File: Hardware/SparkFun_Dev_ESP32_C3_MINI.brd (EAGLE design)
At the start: 21 x 36.1 mm, 88 parts, among them J1 USB Female Type C Connector, J5 Vertical Qwiic Connector, U1 ESP32-C3_MINI-1, U2 RT9080-33GJ5

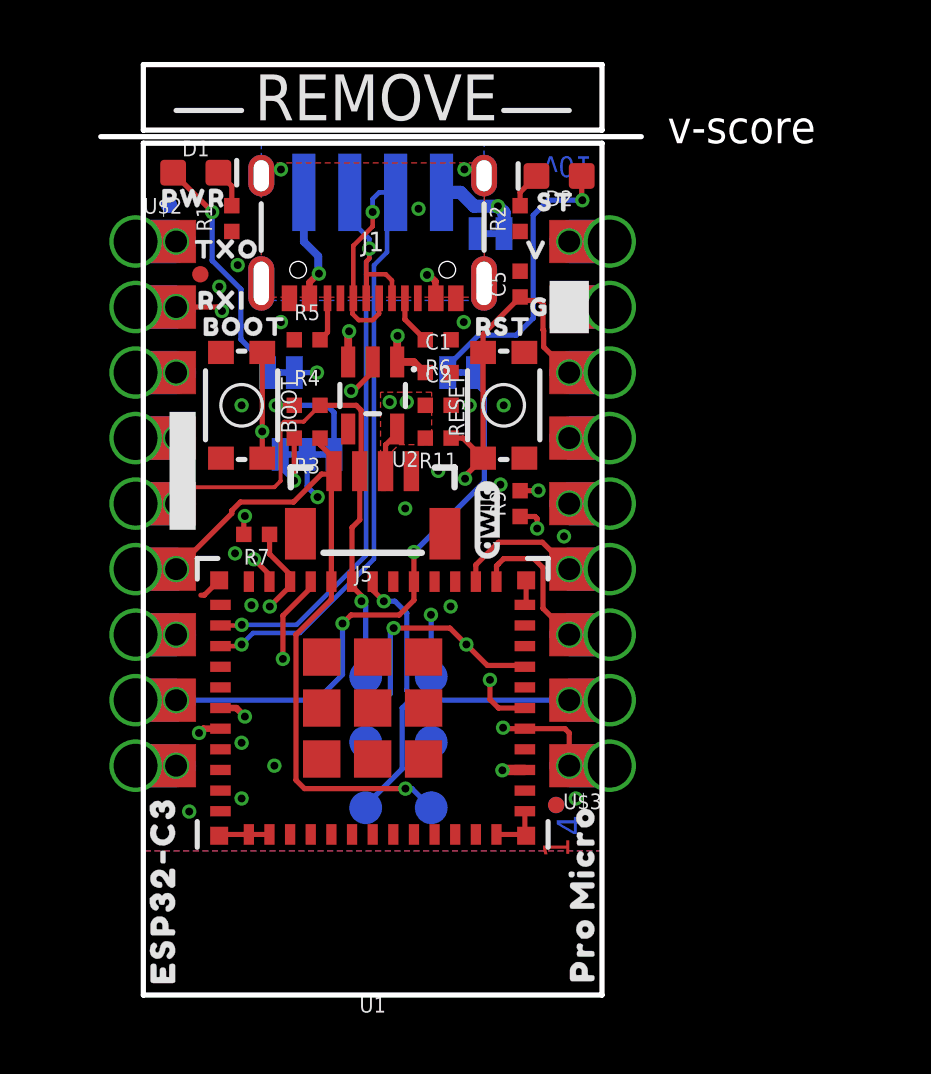
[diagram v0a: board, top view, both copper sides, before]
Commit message: Adds a few vias, cams prototypes
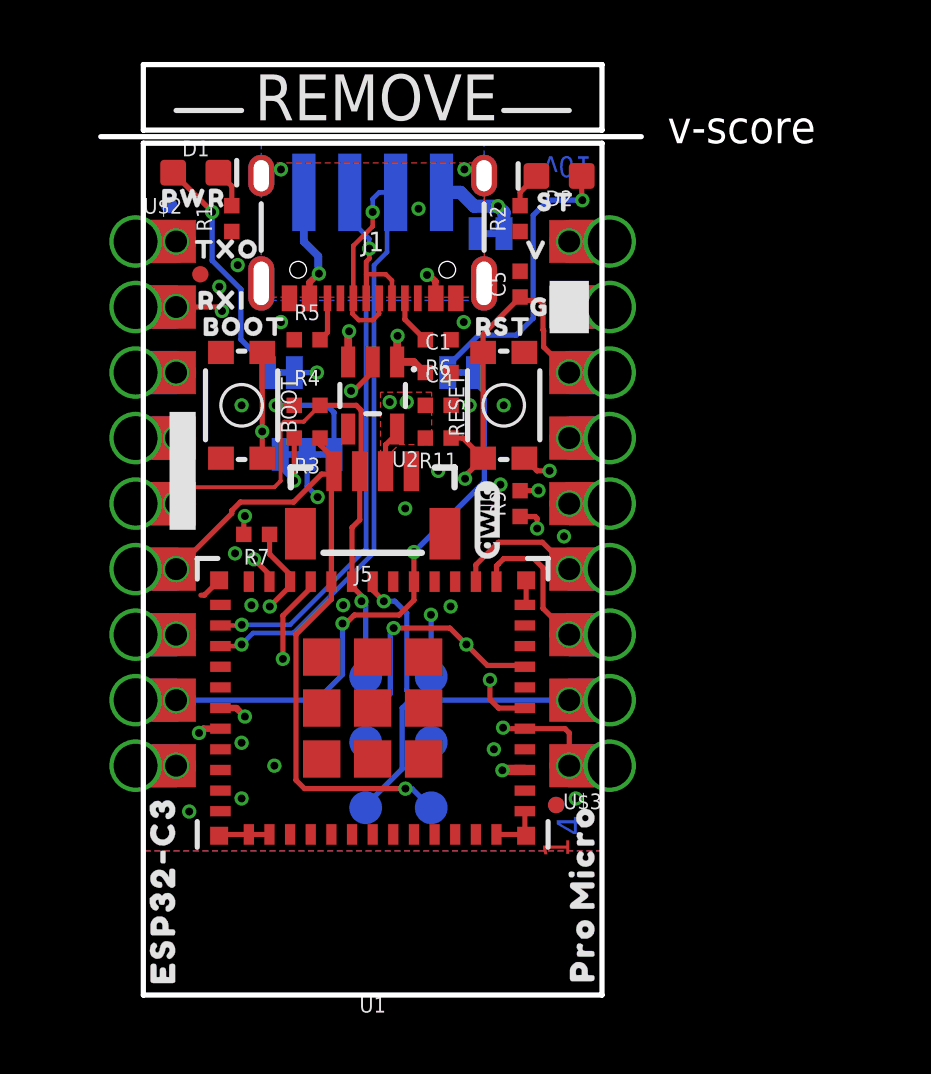
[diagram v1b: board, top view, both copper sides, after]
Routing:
- net GND: track 11.0 -> 12.1 mm, vias 15 -> 22
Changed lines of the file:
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@@
 <layers>
 <layer number="1" name="Top" color="4" fill="1" visible="yes" active="yes"/>
-<layer number="2" name="Route2" color="23" fill="1" visible="no" active="yes"/>
-<layer number="15" name="Route15" color="10" fill="1" visible="no" active="yes"/>
+<layer number="2" name="Route2" color="23" fill="1" visible="yes" active="yes"/>
+<layer number="15" name="Route15" color="10" fill="1" visible="yes" active="yes"/>
 <layer number="16" name="Bottom" color="3" fill="1" visible="yes" active="yes"/>
 <layer number="17" name="Pads" color="26" fill="1" visible="yes" active="yes"/>
@@
 <wire x1="10.029171875" y1="28.934428125" x2="10.029171875" y2="28.543534375" width="0.1778" layer="16"/>
 <wire x1="10.029171875" y1="28.543534375" x2="9.906" y2="28.4203625" width="0.1778" layer="16"/>
-<wire x1="9.906" y1="28.4203625" x2="9.906" y2="17.0482" width="0.1778" layer="16"/>
-<wire x1="9.906" y1="17.0482" x2="7.2088" y2="14.351" width="0.1778" layer="16"/>
-<wire x1="7.2088" y1="14.351" x2="5.0862" y2="14.351" width="0.1778" layer="16"/>
+<wire x1="9.906" y1="28.4203625" x2="9.906" y2="17.3022" width="0.1778" layer="16"/>
+<wire x1="9.906" y1="17.3022" x2="6.9548" y2="14.351" width="0.1778" layer="16"/>
+<wire x1="6.9548" y1="14.351" x2="5.0862" y2="14.351" width="0.1778" layer="16"/>
 <via x="5.0862" y="14.351" extent="1-16" drill="0.3048"/>
 <wire x1="5.0862" y1="14.351" x2="5.0604" y2="14.3252" width="0.1778" layer="1"/>
@@
 <wire x1="10.16" y1="29.7942" x2="10.16" y2="30.353" width="0.1778" layer="1"/>
 <wire x1="9.41" y1="29.0442" x2="10.16" y2="29.7942" width="0.1778" layer="1"/>
-<wire x1="10.2108" y1="16.9034" x2="7.3426" y2="14.0352" width="0.1778" layer="16"/>
+<wire x1="10.2108" y1="17.1574" x2="7.0886" y2="14.0352" width="0.1778" layer="16"/>
 <wire x1="11.049" y1="31.115" x2="10.7188" y2="30.7848" width="0.1778" layer="16"/>
 <wire x1="10.7188" y1="30.7848" x2="10.7188" y2="28.79594375" width="0.1778" layer="16"/>
 <wire x1="10.7188" y1="28.79594375" x2="10.2108" y2="28.28794375" width="0.1778" layer="16"/>
-<wire x1="10.2108" y1="28.28794375" x2="10.2108" y2="16.9034" width="0.1778" layer="16"/>
-<wire x1="7.3426" y1="14.0352" x2="5.5262" y2="14.0352" width="0.1778" layer="16"/>
+<wire x1="10.2108" y1="28.28794375" x2="10.2108" y2="17.1574" width="0.1778" layer="16"/>
+<wire x1="7.0886" y1="14.0352" x2="5.5262" y2="14.0352" width="0.1778" layer="16"/>
 <wire x1="5.08" y1="13.589" x2="5.5262" y2="14.0352" width="0.1778" layer="16"/>
 <wire x1="4.26" y1="13.5252" x2="5.0162" y2="13.5252" width="0.1778" layer="1"/>
@@
 <via x="18.034" y="7.62" extent="1-16" drill="0.3048"/>
 <via x="13.1826" y="15.0622" extent="1-16" drill="0.3048"/>
+<via x="5.08" y="9.779" extent="1-16" drill="0.3048"/>
+<via x="6.35" y="8.89" extent="1-16" drill="0.3048"/>
+<via x="9.017" y="15.113" extent="1-16" drill="0.3048"/>
+<via x="14.859" y="9.525" extent="1-16" drill="0.3048"/>
+<via x="17.5768" y="17.78" extent="1-16" drill="0.3048"/>
+<via x="5.461" y="15.113" extent="1-16" drill="0.3048"/>
+<via x="17.018" y="20.32" extent="1-16" drill="0.3048"/>
+<wire x1="16.04" y1="20.81" x2="16.53" y2="20.32" width="0.2032" layer="1"/>
+<wire x1="16.53" y1="20.32" x2="17.018" y2="20.32" width="0.2032" layer="1"/>
 </signal>
 <signal name="N$4">
@@
 <wire x1="2.54" y1="11.43" x2="8.001" y2="11.43" width="0.2032" layer="16"/>
 <wire x1="11.76" y1="16.0252" x2="11.76" y2="15.3042" width="0.2032" layer="1"/>
-<wire x1="11.1878" y1="14.732" x2="9.3218" y2="14.732" width="0.2032" layer="1"/>
-<wire x1="9.3218" y1="14.732" x2="8.9916" y2="14.4018" width="0.2032" layer="1"/>
+<wire x1="11.1878" y1="14.732" x2="9.4488" y2="14.732" width="0.2032" layer="1"/>
+<wire x1="9.4488" y1="14.732" x2="9.1186" y2="14.4018" width="0.2032" layer="1"/>
+<wire x1="9.1186" y1="14.4018" x2="8.9916" y2="14.4018" width="0.2032" layer="1"/>
 <via x="8.9916" y="14.4018" extent="1-16" drill="0.3048"/>
 <wire x1="11.76" y1="15.3042" x2="11.1878" y2="14.732" width="0.2032" layer="1"/>
@@
 <wire x1="0.97" y1="13.97" x2="2.54" y2="13.97" width="0" layer="19" extent="1-1"/>
 </signal>
-<signal name="N$6">
-<via x="6.35" y="8.89" extent="1-16" drill="0.3048"/>
-</signal>
-<signal name="N$9">
-<via x="5.461" y="15.113" extent="1-16" drill="0.3048"/>
-</signal>
 <signal name="N$13">
 <via x="15.113" y="19.7866" extent="1-16" drill="0.3048"/>
 </signal>
-<signal name="N$14">
-<via x="17.5768" y="17.78" extent="1-16" drill="0.3048"/>
-</signal>
-<signal name="N$15">
-<via x="5.08" y="9.779" extent="1-16" drill="0.3048"/>
-</signal>
 <signal name="N$16">

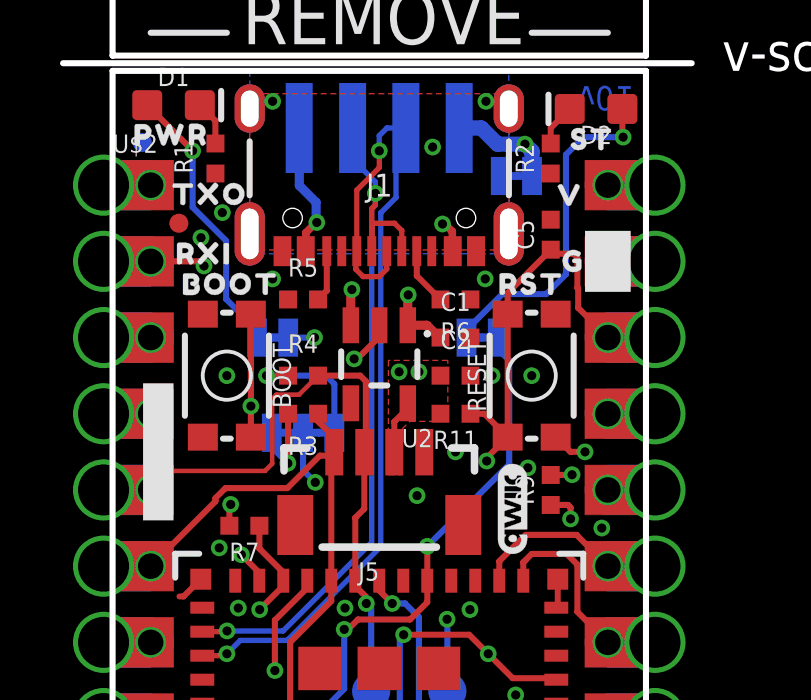
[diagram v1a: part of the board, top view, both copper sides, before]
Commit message: Shortens some nets, fixes some silk
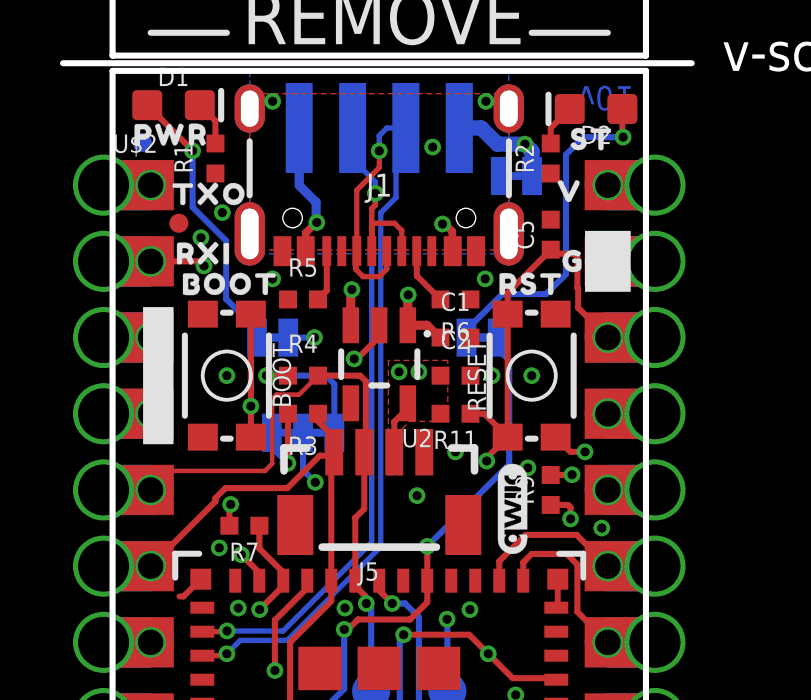
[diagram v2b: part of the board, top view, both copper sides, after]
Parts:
- U$1: device bot:#GND#4 -> prod:G36
- U$10: device bot:#RXI#11 -> prod:TXO40
- U$11: device bot:#TXO#12 -> prod:RXI39
- moved U$1 0.97 mm to (16.6, 26.7)
- moved U$37 0.36 mm to (16.4, 29.0)
- moved U$11 0.36 mm to (4.32, 26.9)
- moved U$10 0.31 mm to (4.37, 28.9)
- moved U$38 0.13 mm to (16.5, 29.0)
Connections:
- net EN renamed !RESET!
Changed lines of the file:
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@@
 <layers>
 <layer number="1" name="Top" color="4" fill="1" visible="yes" active="yes"/>
-<layer number="2" name="Route2" color="23" fill="1" visible="yes" active="yes"/>
-<layer number="15" name="Route15" color="10" fill="1" visible="yes" active="yes"/>
+<layer number="2" name="Route2" color="23" fill="1" visible="no" active="yes"/>
+<layer number="15" name="Route15" color="10" fill="1" visible="no" active="yes"/>
 <layer number="16" name="Bottom" color="3" fill="1" visible="yes" active="yes"/>
 <layer number="17" name="Pads" color="26" fill="1" visible="yes" active="yes"/>
@@
 <text x="17.8054" y="6.5786" size="1.016" layer="16" font="vector" ratio="15" rot="R90" align="center">4</text>
 <rectangle x1="17.018" y1="25.654" x2="18.542" y2="27.686" layer="21"/>
-<rectangle x1="2.286" y1="18.034" x2="3.302" y2="22.606" layer="21"/>
+<rectangle x1="2.286" y1="20.574" x2="3.302" y2="25.146" layer="21"/>
 <rectangle x1="2.159" y1="20.828" x2="4.318" y2="21.59" layer="22"/>
 <rectangle x1="2.159" y1="24.257" x2="4.318" y2="25.019" layer="22"/>
@@
 <attribute name="VALUE" x="10.16" y="17.6252" size="0.6096" layer="27" font="vector" ratio="20" rot="R180" align="center"/>
 </element>
-<element name="U$1" library="bot" package="#GND#4" value="" x="15.748" y="26.289" smashed="yes" rot="MR0"/>
 <element name="U$4" library="bot" package="#GND#4" value="" x="3.81" y="22.86" smashed="yes" rot="MR270"/>
-<element name="U$10" library="bot" package="#RXI#11" value="" x="4.318" y="29.21" smashed="yes" rot="MR0"/>
-<element name="U$11" library="bot" package="#TXO#12" value="" x="4.572" y="26.67" smashed="yes" rot="MR0"/>
 <element name="U$12" library="bot" package="#3V3#0" value="" x="15.875" y="21.59" smashed="yes" rot="MR0"/>
 <element name="U$13" library="prod" package="#A3#PICO#35" value="" x="14.54" y="19.01" smashed="yes" rot="MR0"/>
@@
 <element name="U$35" library="prod" package="PRO0" value="" x="10.16" y="3.81" smashed="yes" rot="MR0"/>
 <element name="U$36" library="prod" package="MICRO1" value="" x="10.16" y="2.54" smashed="yes" rot="MR0"/>
-<element name="U$37" library="prod" package="V35" value="" x="16.637" y="29.21" smashed="yes" rot="MR0"/>
-<element name="U$38" library="prod" package="V35" value="" x="16.5354" y="28.8798" smashed="yes"/>
+<element name="U$37" library="prod" package="V35" value="" x="16.383" y="28.956" smashed="yes" rot="MR0"/>
+<element name="U$38" library="prod" package="V35" value="" x="16.5354" y="29.0068" smashed="yes"/>
 <element name="U$39" library="prod" package="G36" value="" x="16.637" y="26.67" smashed="yes"/>
 <element name="U$41" library="top" package="BOOT15" value="" x="5.207" y="25.908" smashed="yes"/>
@@
 <element name="U$51" library="prod" package="#RT#45" value="" x="16.2306" y="24.13" smashed="yes" rot="MR0"/>
 <element name="U$5" library="prod" package="RST41" value="" x="15.24" y="25.908" smashed="yes"/>
+<element name="U$10" library="prod" package="TXO40" value="" x="4.3688" y="28.9052" smashed="yes" rot="MR0"/>
+<element name="U$11" library="prod" package="RXI39" value="" x="4.318" y="26.924" smashed="yes" rot="MR0"/>
+<element name="U$1" library="prod" package="G36" value="" x="16.637" y="26.67" smashed="yes" rot="MR0"/>
 </elements>
 <signals>
@@
 <wire x1="17.78" y1="29.21" x2="19.35" y2="29.21" width="0" layer="19" extent="1-1"/>
 </signal>
-<signal name="EN">
+<signal name="!RESET!">
 <contactref element="R11" pad="1"/>
 <contactref element="RESET" pad="3"/>

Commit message: Renames I2S pins
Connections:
- net IOA4/MTMS renamed IOA4/MTMS/I2S_BCK
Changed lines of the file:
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@@
 <wire x1="6.16" y1="16.2936" x2="5.5626" y2="16.891" width="0.2032" layer="1"/>
 </signal>
-<signal name="IOA4/MTMS">
+<signal name="IOA4/MTMS/I2S_BCK">
 <contactref element="U$3" pad="8B"/>
 <contactref element="U$3" pad="8"/>

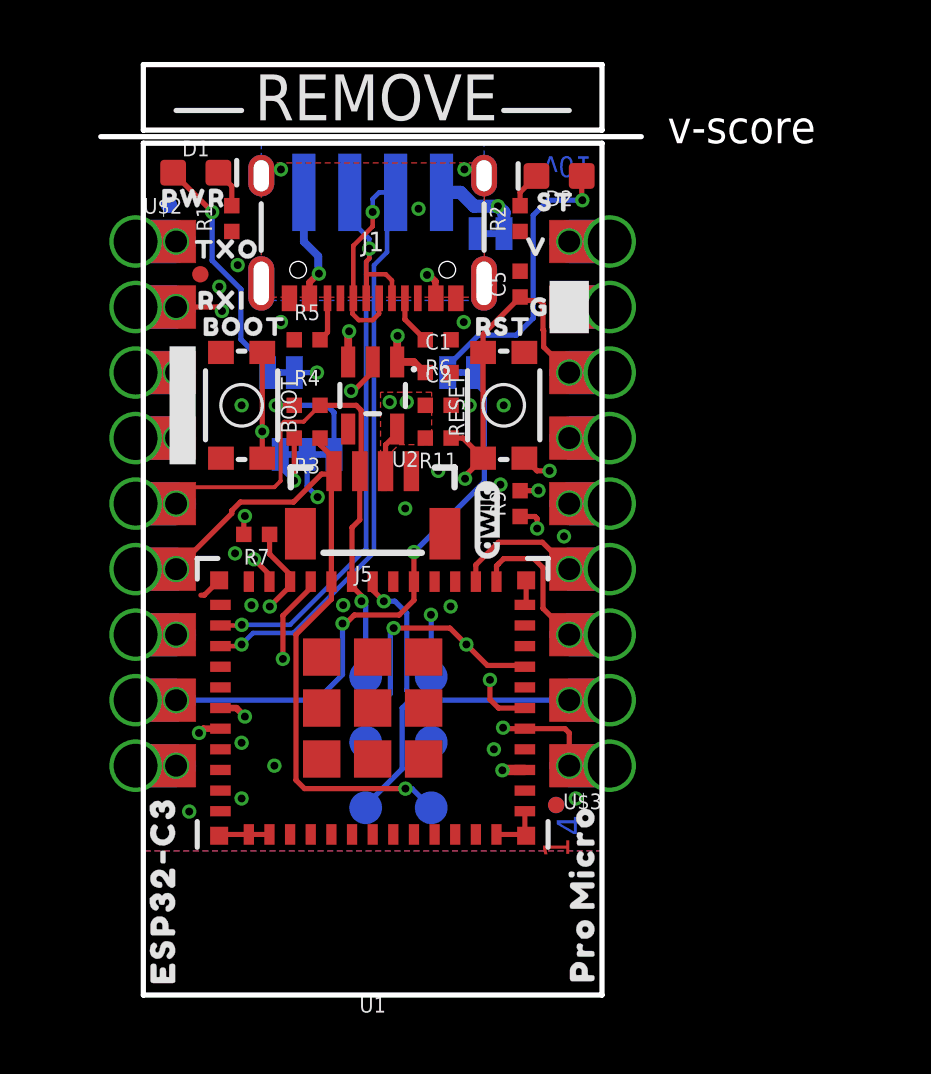
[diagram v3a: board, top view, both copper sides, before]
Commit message: Adds numerous aesthetic changes
* Increases size of silk everywhere possible
* Moves jumpers for LEDs to the corners underneath the respective LED.
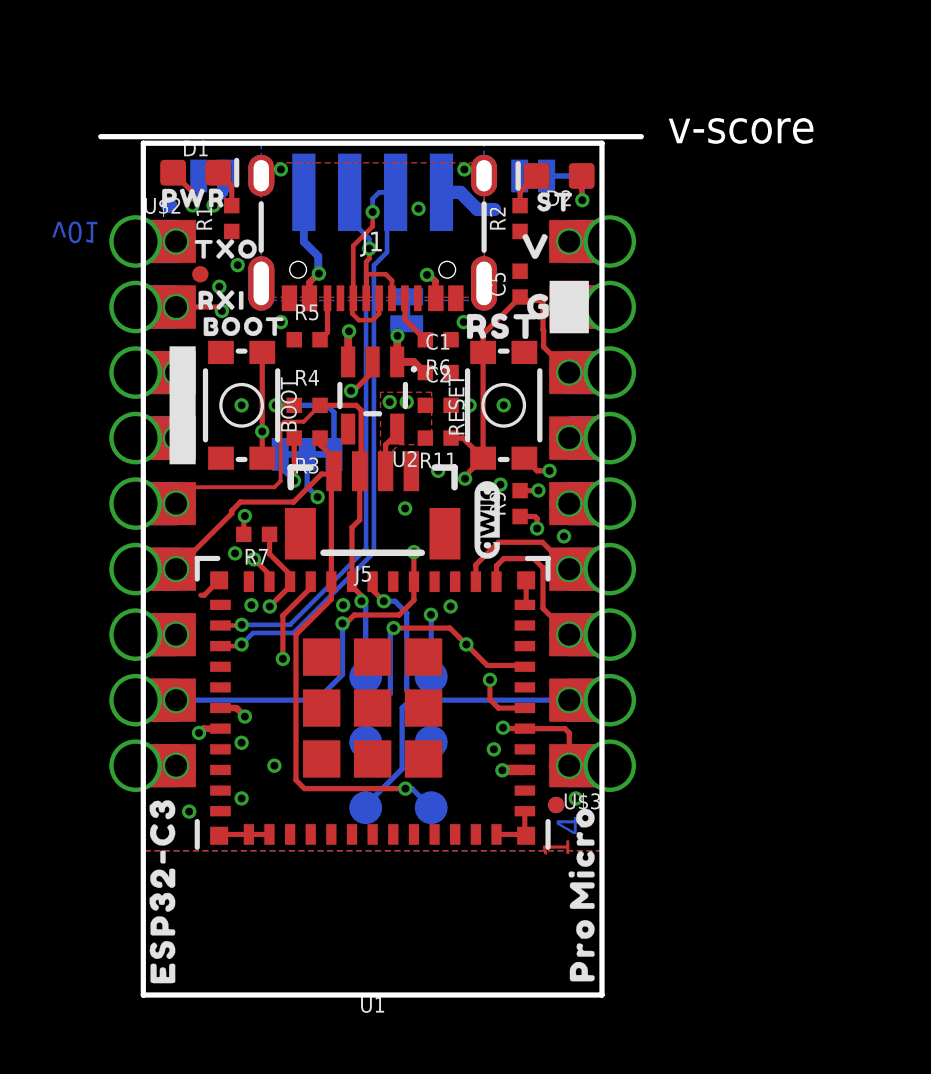
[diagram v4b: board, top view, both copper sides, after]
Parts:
- removed U$51: (no value), prod:#RT#45
- added U$40: (no value), prod:#A3#PICO#45
- D1: value RED -> Red
- D2: value BLUE -> Blue
- U$12: device bot:#3V3#0 -> prod:#8#50
- U$13: device prod:#A3#PICO#35 -> prod:#A1#POCI#50
- U$14: device prod:#A1#POCI#35 -> prod:#A0#SCLK#50
- U$15: device prod:#A2#35 -> prod:#A4#50
- U$16: device prod:#A0#SCLK#35 -> prod:#A2#50
- U$17: device prod:#A4#35 -> prod:#RT#44
- U$18: device prod:#8#35 -> prod:#5#SDA#50
- U$19: device prod:#10#FS#35 -> prod:#6#SCL#50
- U$20: device prod:#5#SDA#SDI#49 -> prod:#7#50
- U$21: device prod:#6#SCL#SCK#49 -> prod:#10#50
- U$22: device prod:#7#SDO#49 -> top:#GND#4
- U$4: device bot:#GND#4 -> top:#3V3#0
- U$7: device prod:#PWR#47 -> prod:#P#49
- U$8: device prod:#STAT#48 -> prod:#S#51
- moved U$12 17.4 mm to (3.94, 8.89)
- moved U$17 12.7 mm to (15.9, 24.1)
- moved U$4 11.6 mm to (15.4, 21.6), turned to 0 degrees
- moved U$7 10.8 mm to (2.03, 31.8)
- moved U$18 10.5 mm to (5.84, 19.1)
- moved U$8 10.3 mm to (18.3, 31.8)
- moved U$22 9.08 mm to (4.01, 23.0), turned to 270 degrees
- moved STAT 8.12 mm to (16.4, 31.8), turned to 0 degrees
- moved PWR 8.07 mm to (3.94, 31.8)
- moved LOGO3 7.90 mm to (3.17, 1.65)
- moved U$9 5.66 mm to (13.5, 26.0), turned to 0 degrees
- moved U$20 5.57 mm to (3.94, 14.0)
- moved U$21 5.52 mm to (4.19, 11.4)
- moved U$16 5.25 mm to (15.9, 8.89)
- moved U$19 5.11 mm to (5.59, 16.5)
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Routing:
- net N$11: track 11.4 -> 2.98 mm
- net IO10/I2S_FS: track 22.5 -> 14.5 mm
- net N$2: track 9.26 -> 3.19 mm
- net GND: track 12.1 -> 10.9 mm, vias 22 -> 21
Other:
- board size 21 x 36.1 mm -> 21 x 33.3 mm
- board text removed: "REMOVE"
